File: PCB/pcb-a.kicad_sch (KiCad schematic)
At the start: 30 parts, among them Q1 BC327, Q3 BC337, SW1 config, U1 MCP23008-xP, U2 MAX232I, U4 ATmega16L-8P, Y1 8Mhz

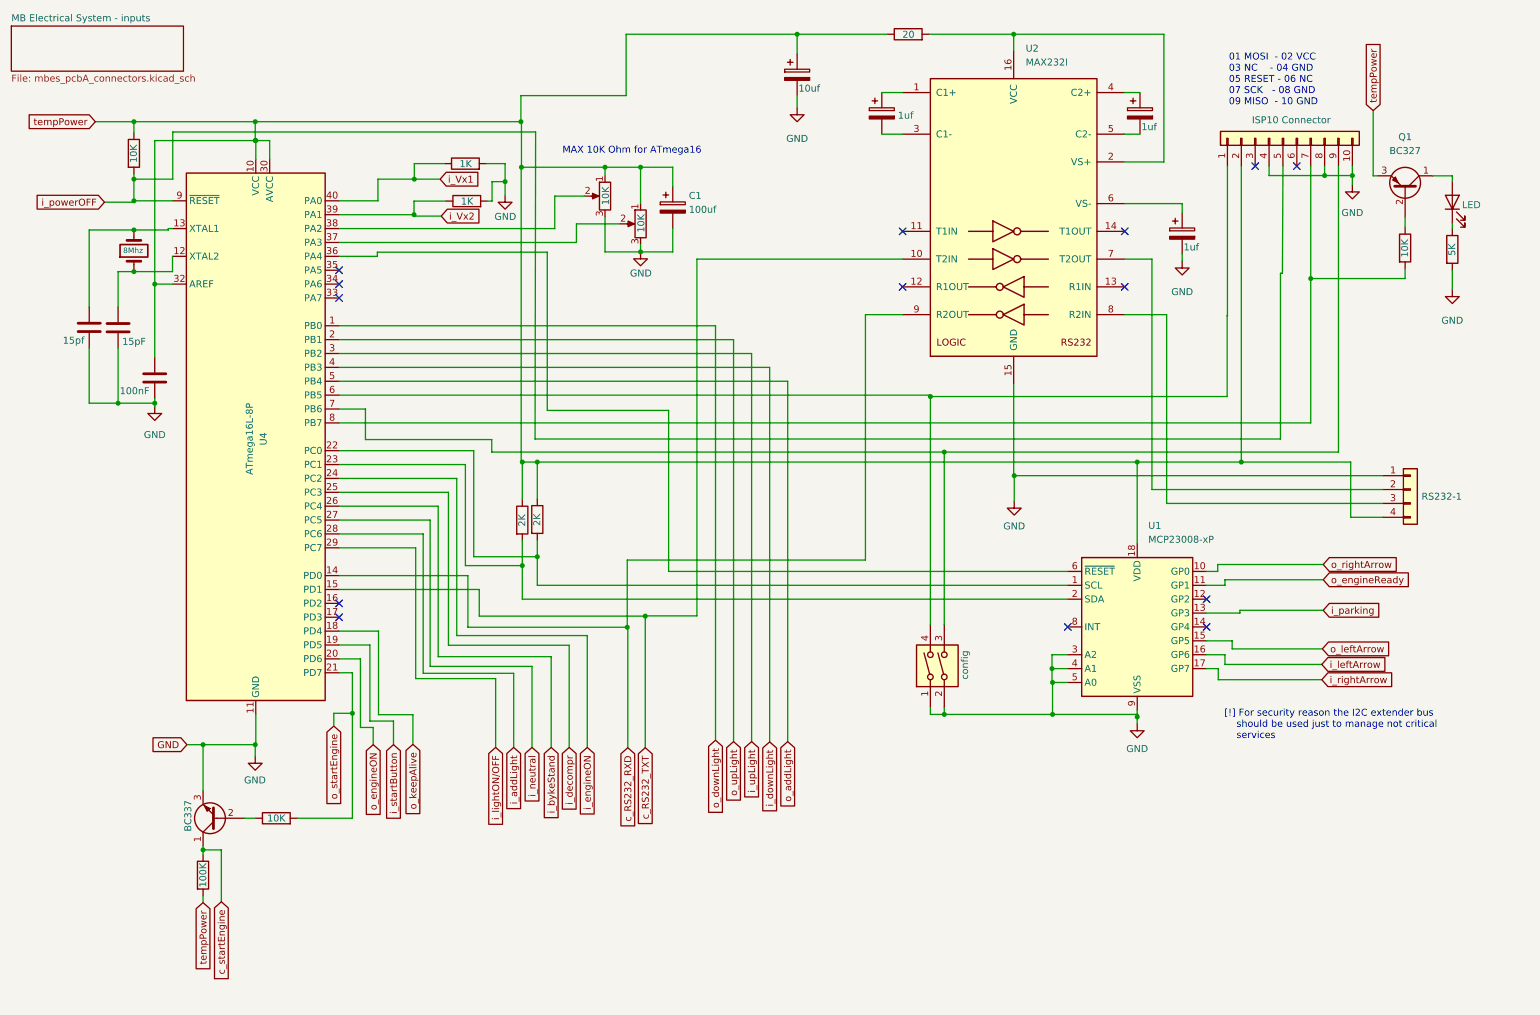
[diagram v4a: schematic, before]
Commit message: No USB support and PCB-B size reducing
Implementing USB power support using 7805 was a stupid idea: too much wasted electic current in Joule effect. So, I moved just
one 7805 in the PCB-A, because the its used power is very low. It allowed me to optimize the PCB-B used space and reduce its
whole size ;-)
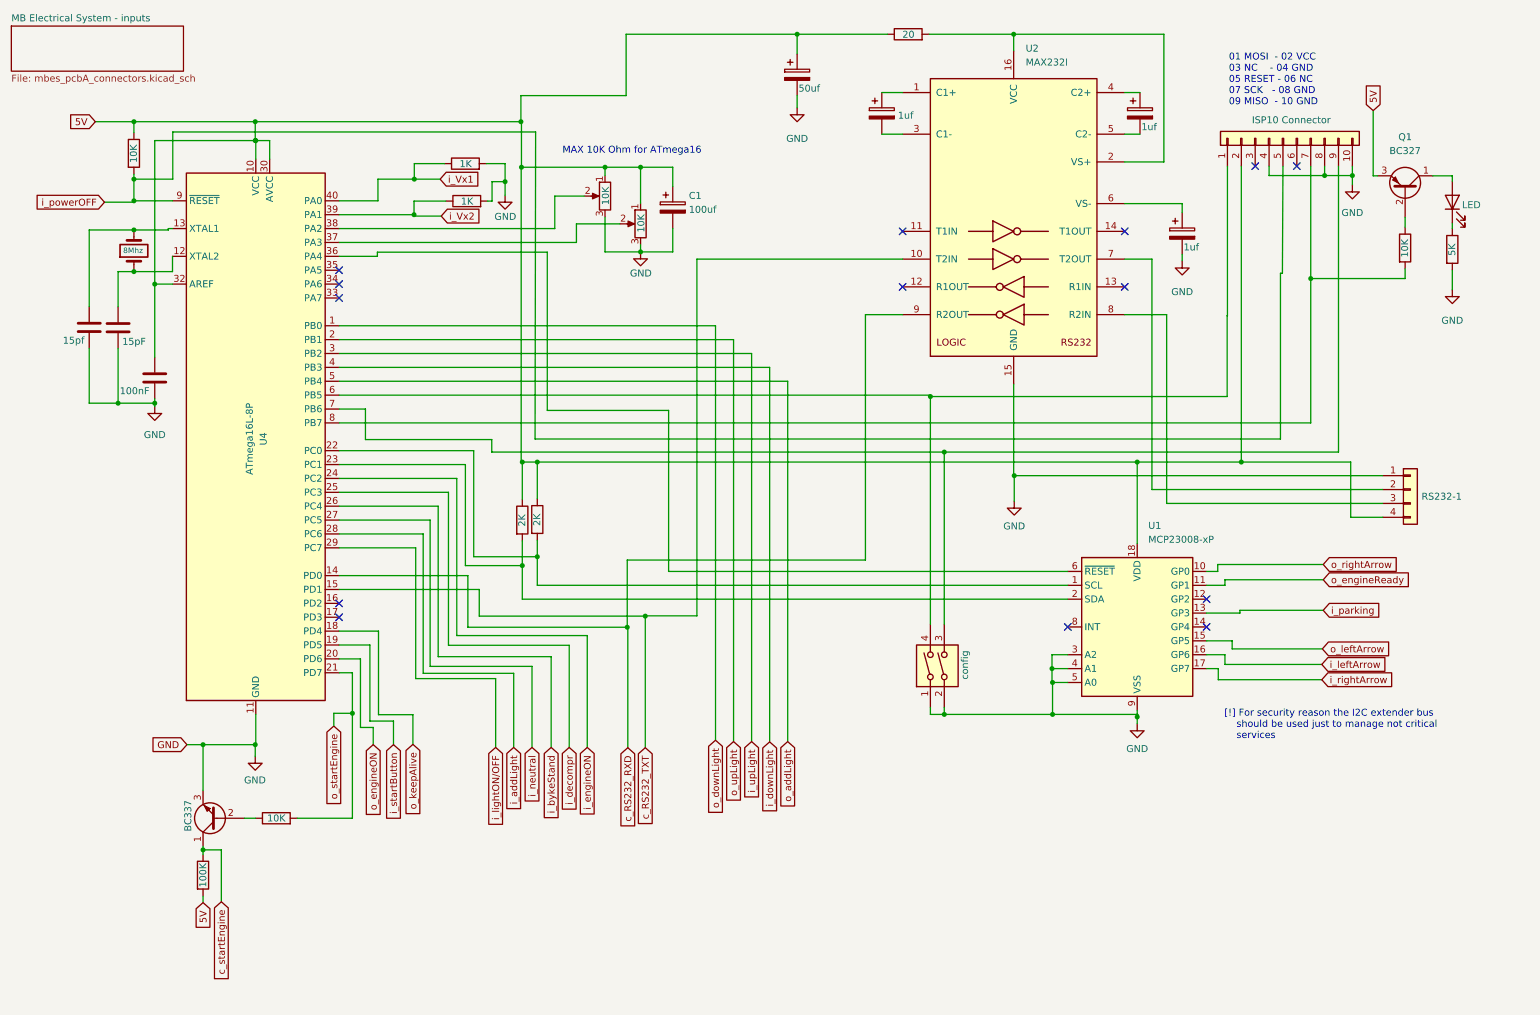
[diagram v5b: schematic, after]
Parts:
- C7: value 10uf -> 50uf
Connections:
- net tempPower renamed 5V
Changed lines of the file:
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@@
 		)
 	)
-	(global_label "tempPower"
+	(global_label "5V"
 		(shape input)
 		(at 29.8196 35.306 180)
@@
 		)
 		(property "Intersheetrefs" "${INTERSHEET_REFS}"
-			(at 29.8196 35.306 0)
-			(effects
-				(font
-					(size 1.27 1.27)
-				)
-				(hide yes)
-			)
-		)
-		(property "Riferimenti inter-foglio" "${INTERSHEET_REFS}"
-			(at 17.1255 35.3854 0)
+			(at 24.5363 35.306 0)
+			(effects
+				(font
+					(size 1.27 1.27)
+				)
+				(justify right)
+				(hide yes)
+			)
+		)
+		(property "Riferimenti inter-foglio" "${INTERSHEET_REFS}"
+			(at 29.8196 37.4968 0)
 			(effects
 				(font
@@
 		)
 	)
-	(global_label "tempPower"
+	(global_label "5V"
 		(shape input)
 		(at 263.652 33.274 90)
@@
 		)
 		(property "Intersheetrefs" "${INTERSHEET_REFS}"
-			(at 263.652 20.0079 90)
+			(at 263.652 27.9907 90)
 			(effects
 				(font
@@
 		)
 	)
-	(global_label "tempPower"
+	(global_label "5V"
 		(shape input)
 		(at 49.53 178.2064 270)
@@
 		)
 		(property "Intersheetrefs" "${INTERSHEET_REFS}"
-			(at 49.53 178.2064 0)
-			(effects
-				(font
-					(size 1.27 1.27)
-				)
-				(hide yes)
-			)
-		)
-		(property "Riferimenti inter-foglio" "${INTERSHEET_REFS}"
-			(at 49.6094 190.9005 90)
+			(at 49.53 183.4897 90)
+			(effects
+				(font
+					(size 1.27 1.27)
+				)
+				(justify right)
+				(hide yes)
+			)
+		)
+		(property "Riferimenti inter-foglio" "${INTERSHEET_REFS}"
+			(at 51.7208 178.2064 90)
 			(effects
 				(font
@@
 			)
 		)
-		(property "Value" "10uf"
+		(property "Value" "50uf"
 			(at 158.496 29.21 0)
 			(effects

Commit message: External power connector, and one 100nF cap. added
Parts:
- added C9: 100nF, Capacitor_THT:C_Disc_D6.0mm_W2.5mm_P5.00mm, symbol Device:C
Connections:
- net 5V: now also C9.1
- net GND: now also C9.2
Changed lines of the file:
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@@
 	)
 	(junction
+		(at 239.522 66.802)
+		(diameter 0)
+		(color 0 0 0 0)
+	)
+	(junction
 		(at 123.0884 43.6372)
 		(diameter 0)
@@
 	)
 	(junction
+		(at 278.13 66.802)
+		(diameter 0)
+		(color 0 0 0 0)
+	)
+	(junction
 		(at 59.0804 38.7604)
 		(diameter 0)
@@
 	(wire
 		(pts
+			(xy 264.16 66.802) (xy 239.522 66.802)
+		)
+		(stroke
+			(width 0)
+			(type default)
+		)
+	)
+	(wire
+		(pts
 			(xy 126.9492 30.5308) (xy 107.696 30.5308)
 		)
@@
 	(wire
 		(pts
+			(xy 271.78 66.802) (xy 278.13 66.802)
+		)
+		(stroke
+			(width 0)
+			(type default)
+		)
+	)
+	(wire
+		(pts
 			(xy 74.422 90.424) (xy 252.222 90.424)
 		)
@@
 	(wire
 		(pts
+			(xy 239.522 66.802) (xy 239.522 97.5868)
+		)
+		(stroke
+			(width 0)
+			(type default)
+		)
+	)
+	(wire
+		(pts
 			(xy 225.3488 42.672) (xy 225.3488 19.304)
 		)
@@
 	(wire
 		(pts
-			(xy 278.13 62.484) (xy 278.13 66.04)
+			(xy 278.13 62.484) (xy 278.13 66.802)
 		)
 		(stroke
@@
 	(wire
 		(pts
-			(xy 239.522 43.434) (xy 239.522 97.5868)
+			(xy 239.522 43.434) (xy 239.522 66.802)
 		)
 		(stroke
@@
 	(wire
 		(pts
+			(xy 278.13 66.802) (xy 278.13 75.946)
+		)
+		(stroke
+			(width 0)
+			(type default)
+		)
+	)
+	(wire
+		(pts
 			(xy 218.186 37.592) (xy 220.98 37.592)
 		)
@@
 	(symbol
 		(lib_id "power:GND")
-		(at 278.13 66.04 0)
+		(at 278.13 75.946 0)
 		(unit 1)
 		(exclude_from_sim no)
@@
 		(fields_autoplaced yes)
 		(property "Reference" "#PWR04"
-			(at 278.13 72.39 0)
+			(at 278.13 82.296 0)
 			(effects
 				(font
@@
 		)
 		(property "Value" "GND"
-			(at 278.13 71.6788 0)
+			(at 278.13 81.5848 0)
 			(effects
 				(font
@@
 		)
 		(property "Footprint" ""
-			(at 278.13 66.04 0)
+			(at 278.13 75.946 0)
 			(effects
 				(font
@@
 		)
 		(property "Datasheet" ""
-			(at 278.13 66.04 0)
+			(at 278.13 75.946 0)
 			(effects
 				(font
@@
 		)
 		(property "Description" ""
-			(at 278.13 66.04 0)
+			(at 278.13 75.946 0)
 			(effects
 				(font
@@
 					(unit 1)
 				)
+			)
+		)
+	)
+	(symbol
+		(lib_id "Device:C")
+		(at 267.97 66.802 90)
+		(unit 1)
+		(exclude_from_sim no)
+		(in_bom yes)
+		(on_board yes)
+		(dnp no)
+		(property "Reference" "C9"
+			(at 266.6999 62.9412 0)
+			(effects
+				(font
+					(size 1.27 1.27)
+				)
+				(justify left)
+				(hide yes)
+			)
+		)
+		(property "Value" "100nF"
+			(at 266.192 68.326 90)
+			(effects
+				(font
+					(size 1.27 1.27)
+				)
+				(justify left)
+			)
+		)
+		(property "Footprint" "Capacitor_THT:C_Disc_D6.0mm_W2.5mm_P5.00mm"
+			(at 271.78 65.8368 0)
+			(effects
+				(font
+					(size 1.27 1.27)
+				)
+				(hide yes)
+			)
+		)
+		(property "Datasheet" "~"
+			(at 267.97 66.802 0)
+			(effects
+				(font
+					(size 1.27 1.27)
+				)
+				(hide yes)
+			)
+		)
+		(property "Description" ""
+			(at 267.97 66.802 0)
+			(effects
+				(font
+					(size 1.27 1.27)
+				)
+				(hide yes)
+			)
+		)
+		(pin "1"
+		)
+		(pin "2"
+		)
+		(instances
+			(project "pcb-a"
+				(path "/709d0967-afe5-49d3-92a5-d2bb94550bdb"
+					(reference "C9")
+					(unit 1)
+				)

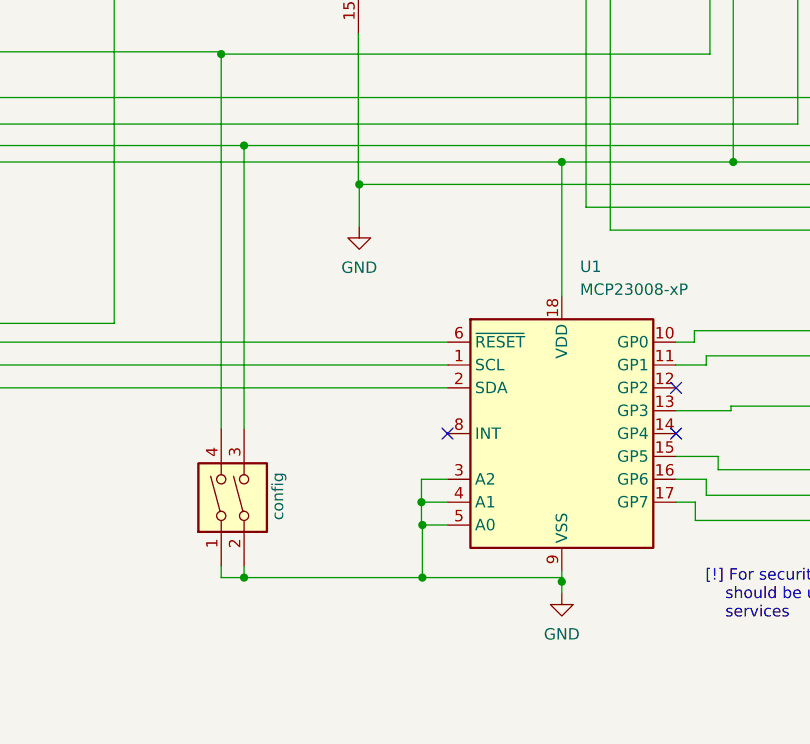
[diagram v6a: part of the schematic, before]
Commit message: Small cap added for MCP23008 dev
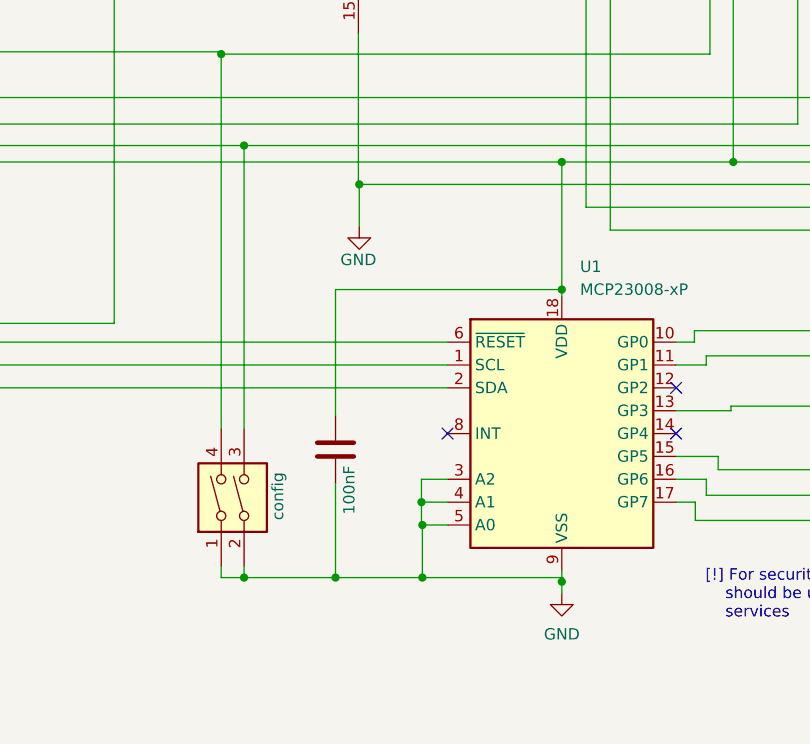
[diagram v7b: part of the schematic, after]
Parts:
- added C10: 100nF, Capacitor_THT:C_Disc_D6.0mm_W2.5mm_P5.00mm, symbol Device:C
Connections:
- net 5V: now also C10.2
- net GND: now also C10.1
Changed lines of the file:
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@@
 	)
 	(junction
+		(at 195.326 143.764)
+		(diameter 0)
+		(color 0 0 0 0)
+	)
+	(junction
 		(at 182.626 85.598)
 		(diameter 0)
@@
 	)
 	(junction
+		(at 220.472 111.76)
+		(diameter 0)
+		(color 0 0 0 0)
+	)
+	(junction
 		(at 197.9676 100.076)
 		(diameter 0)
@@
 	(wire
 		(pts
+			(xy 195.326 125.73) (xy 195.326 111.76)
+		)
+		(stroke
+			(width 0)
+			(type default)
+		)
+	)
+	(wire
+		(pts
 			(xy 74.422 118.364) (xy 97.9932 118.364)
 		)
@@
 	(wire
 		(pts
+			(xy 195.326 133.35) (xy 195.326 143.764)
+		)
+		(stroke
+			(width 0)
+			(type default)
+		)
+	)
+	(wire
+		(pts
 			(xy 61.722 42.164) (xy 61.722 38.7604)
 		)
@@
 	(wire
 		(pts
+			(xy 220.472 111.76) (xy 220.472 112.522)
+		)
+		(stroke
+			(width 0)
+			(type default)
+		)
+	)
+	(wire
+		(pts
 			(xy 88.1888 42.9768) (xy 88.1888 45.8216)
 		)
@@
 	(wire
 		(pts
+			(xy 195.326 143.764) (xy 204.978 143.764)
+		)
+		(stroke
+			(width 0)
+			(type default)
+		)
+	)
+	(wire
+		(pts
 			(xy 107.95 122.682) (xy 107.95 116.5352)
 		)
@@
 	(wire
 		(pts
+			(xy 195.326 111.76) (xy 220.472 111.76)
+		)
+		(stroke
+			(width 0)
+			(type default)
+		)
+	)
+	(wire
+		(pts
 			(xy 218.186 50.292) (xy 228.7016 50.292)
 		)
@@
 	(wire
 		(pts
-			(xy 185.166 143.764) (xy 204.978 143.764)
+			(xy 185.166 143.764) (xy 195.326 143.764)
 		)
 		(stroke
@@
 	(wire
 		(pts
-			(xy 220.472 97.5868) (xy 220.472 112.522)
+			(xy 220.472 97.5868) (xy 220.472 111.76)
 		)
 		(stroke
@@
 		)
 		(property "Value" "GND"
-			(at 197.9676 109.3216 0)
+			(at 197.866 108.458 0)
 			(effects
 				(font
@@
 					(unit 1)
 				)
+			)
+		)
+	)
+	(symbol
+		(lib_id "Device:C")
+		(at 195.326 129.54 180)
+		(unit 1)
+		(exclude_from_sim no)
+		(in_bom yes)
+		(on_board yes)
+		(dnp no)
+		(property "Reference" "C10"
+			(at 191.4652 130.8101 0)
+			(effects
+				(font
+					(size 1.27 1.27)
+				)
+				(justify left)
+				(hide yes)
+			)
+		)
+		(property "Value" "100nF"
+			(at 196.85 131.318 90)
+			(effects
+				(font
+					(size 1.27 1.27)
+				)
+				(justify left)
+			)
+		)
+		(property "Footprint" "Capacitor_THT:C_Disc_D6.0mm_W2.5mm_P5.00mm"
+			(at 194.3608 125.73 0)
+			(effects
+				(font
+					(size 1.27 1.27)
+				)
+				(hide yes)
+			)
+		)
+		(property "Datasheet" "~"
+			(at 195.326 129.54 0)
+			(effects
+				(font
+					(size 1.27 1.27)
+				)
+				(hide yes)
+			)
+		)
+		(property "Description" ""
+			(at 195.326 129.54 0)
+			(effects
+				(font
+					(size 1.27 1.27)
+				)
+				(hide yes)
+			)
+		)
+		(pin "1"
+		)
+		(pin "2"
+		)
+		(instances
+			(project "pcb-a"
+				(path "/709d0967-afe5-49d3-92a5-d2bb94550bdb"
+					(reference "C10")
+					(unit 1)
+				)

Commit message: Old files replaced.
They have been merged for error
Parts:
- removed C1: 100uf, Capacitor_THT:CP_Radial_D8.0mm_P2.50mm, symbol Device:C_Polarized
- removed C10, C2, C9: 100nF, Capacitor_THT:C_Disc_D6.0mm_W2.5mm_P5.00mm, symbol Device:C
- removed C3: 15pf, Capacitor_THT:C_Disc_D6.0mm_W2.5mm_P5.00mm, symbol Device:C
- removed C4: 15pF, Capacitor_THT:C_Disc_D6.0mm_W2.5mm_P5.00mm, symbol Device:C
- removed C5, C6, C8: 1uf, Capacitor_THT:CP_Radial_D8.0mm_P2.50mm, symbol Device:C_Polarized
- removed C7: 50uf, Capacitor_THT:CP_Radial_D8.0mm_P2.50mm, symbol Device:C_Polarized
- removed D1: LED, LED_THT:LED_D3.0mm, symbol Device:LED
- removed ISP101: ISP10 Connector, Connector_PinHeader_2.54mm:PinHeader_2x05_P2.54mm_Vertical, symbol Connector_Generic:Conn_01x10
- removed Q1: BC327, Package_TO_SOT_THT:TO-92_Inline_Wide, symbol Transistor_BJT:BC327
- removed R10: 2K, Resistor_THT:R_Axial_DIN0204_L3.6mm_D1.6mm_P5.08mm_Horizontal, symbol Device:R
- removed R11: 20, Resistor_THT:R_Axial_DIN0204_L3.6mm_D1.6mm_P5.08mm_Horizontal, symbol Device:R
- removed R9: 5K, Resistor_THT:R_Axial_DIN0204_L3.6mm_D1.6mm_P5.08mm_Horizontal, symbol Device:R
- removed RS232-1: Conn_01x04, Connector_PinHeader_2.54mm:PinHeader_1x04_P2.54mm_Vertical, symbol Connector_Generic:Conn_01x04
- removed U1: MCP23008-xP, Package_DIP:DIP-18_W7.62mm, symbol Interface_Expansion:MCP23008-xP
- removed U2: MAX232I, Package_DIP:CERDIP-16_W7.62mm_SideBrazed_LongPads, symbol Interface_UART:MAX232I
- removed U4: ATmega16L-8P, Package_DIP:DIP-40_W15.24mm, symbol ATmega:ATmega16L-8P
- removed Y1: 8Mhz, Crystal:Crystal_HC49-U_Vertical, symbol Device:Crystal
- added U1: ESP32-S2-DevKitM, PCM_Espressif:ESP32-S2-DevKitM, symbol PCM_Espressif:ESP32-S2-DevKitM
- R2, R8: value 10K -> 100K
- R5: value 2K -> 100K
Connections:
- net GND: now also R3.1, R4.1, RV1.1, SW1.3, SW1.4, U1.21 (GND), U1.42 (GND); no longer R3.2, R4.2, RV1.3, SW1.1, SW1.2
- net i_Vx1: now also R3.2, U1.3 (GPIO1/TOUCH1/ADC1_CH0); no longer R3.1
- net i_Vx2: now also R4.2, U1.4 (GPIO2/TOUCH2/ADC1_CH1); no longer R4.1
- net i_addLight: now also U1.25 (GPIO21)
- net i_bykeStand: now also U1.36 (MTMS/JTAG/GPIO42)
- net i_decompr: now also U1.37 (U0TXD/GPIO43/CLK_OUT1)
- net i_downLight: now also U1.29 (GPIO35)
- net i_engineON: now also U1.38 (U0RXD/GPIO44/CLK_OUT2)
- net i_leftArrow: now also U1.40 (GPIO46/LOG)
- net i_lightON/OFF: now also U1.2 (GPIO0/BOOT)
- net i_neutral: now also U1.13 (GPIO11/TOUCH11/ADC2_CH0/FSPID/FSPIIO5)
- net i_powerOFF: now also R2.1, U1.41 (~{RST}); no longer R2.2
- net i_rightArrow: now also U1.27 (GPIO33)
- net i_startButton: now also U1.39 (GPIO45/VSPI)
- net i_upLight: now also U1.30 (GPIO36)
- net o_addLight: now also U1.28 (GPIO34)
- net o_downLight: now also U1.32 (GPIO38)
- net o_engineON: now also U1.18 (GPIO16/U0CTS/ADC2_CH5/XTAL_32K_N)
- net o_engineReady: now also U1.15 (GPIO13/TOUCH13/ADC2_CH2/FSPIQ/FSPIIO7)
- net o_keepAlive: now also U1.14 (GPIO12/TOUCH12/ADC2_CH1/FSPICLK/FSPIIO6)
- net o_leftArrow: now also U1.22 (GPIO18/U1RXD/ADC2_CH7/DAC_2/CLK_OUT3/RGB_LED)
- net o_rightArrow: now also U1.33 (MTCK/JTAG/GPIO39)
- net o_startEngine: now also U1.34 (MTDO/JTAG/GPIO40)
- net o_upLight: now also U1.31 (GPIO37)
- net at R5.2: now also SW1.2, U1.12 (GPIO10/TOUCH10/ADC1_CH9/FSPICS0/FSPIIO4)
- net at RV2.2: now also U1.6 (GPIO4/TOUCH4/ADC1_CH3)
- net at RV1.2: now also U1.5 (GPIO3/TOUCH3/ADC1_CH2)
- net at R8.2: now also SW1.1, U1.11 (GPIO9/TOUCH9/ADC1_CH8/FSPIHD)
- net tempPower: now reaches R8.1
- net tempPower: now also R2.2, R5.1, R6.2, RV1.3, RV2.1, U1.20 (5V0)
- removed net 5V: R2.1, R5.1, R6.2, RV1.1, RV2.1
- new net i_clutch: U1.35 (MTDI/JTAG/GPIO41)
- new net i_horn: U1.19 (GPIO17/U1TXD/ADC2_CH6/DAC_1)
- new net o_horn: U1.26 (GPIO26)
- new net o_neutral: U1.16 (GPIO14/TOUCH14/ADC2_CH3/FSPIWP/FSPIDQS)
- no-connect marks 14 -> 8
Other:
- added sheet MB Electrical System - rear side connector (mbes_rear_connector.kicad_sch)
- added sheet conn_to_PCBB (conn_to_pcbb.kicad_sch)
- sheet MB Electrical System - inputs: file mbes_pcbA_connectors.kicad_sch -> mbes_inputs.kicad_sch
- note removed: "01 MOSI - 02 VCC 03 NC - 04 GND 05 RESET - 06 NC 07 SCK - 08 GND 09 MISO - 10 GND"
- note removed: "MAX 10K Ohm for ATmega16"
- note removed: "[!] For security reason the I2C extender bus should be used just to manage not critical services"
